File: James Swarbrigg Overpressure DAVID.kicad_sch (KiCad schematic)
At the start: 20 parts, among them J1 Screw_Terminal_01x02, J2 Screw_Terminal_01x02, J3 Fuse Holder 200mA, J4 Screw_Terminal_01x02, K1 G5V-2, Q1 BC184L, U2 TSR_1-2450, U3 LM358N

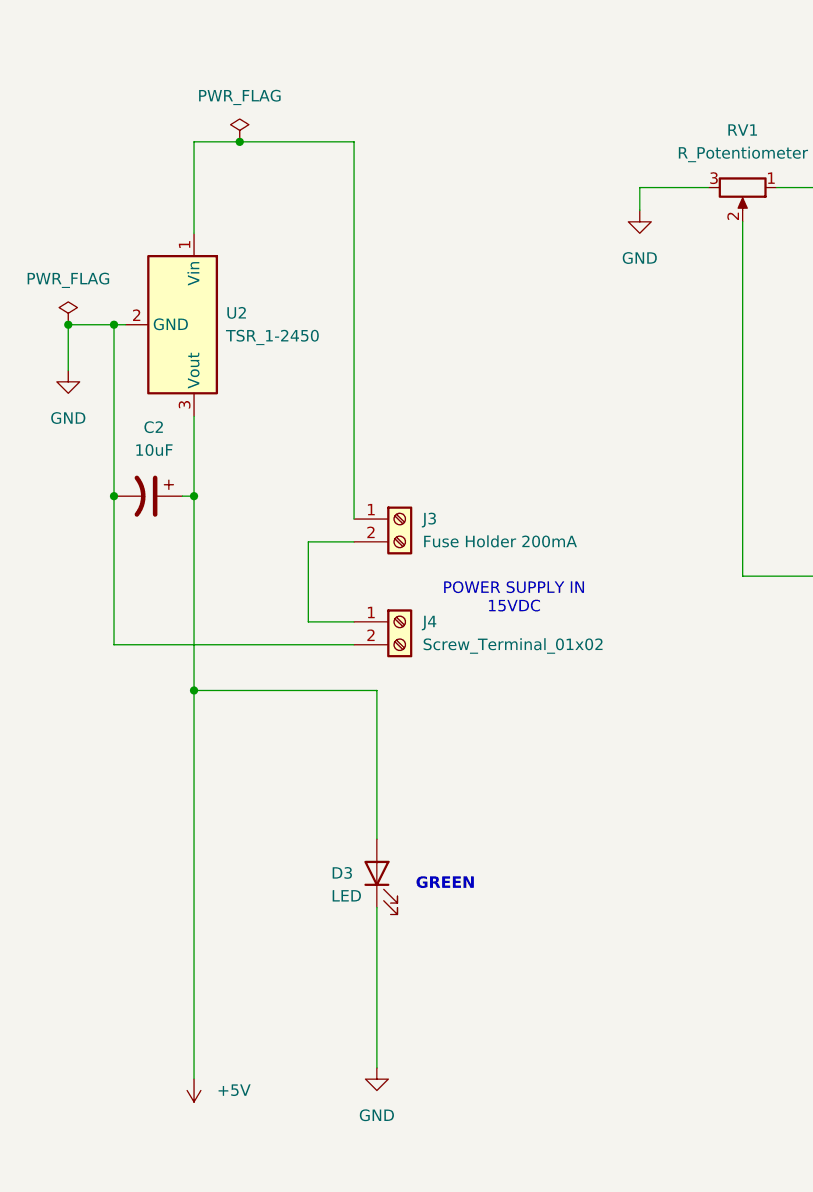
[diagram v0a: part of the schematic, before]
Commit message: Update overpressure cutout PCB and add Gerbers V1
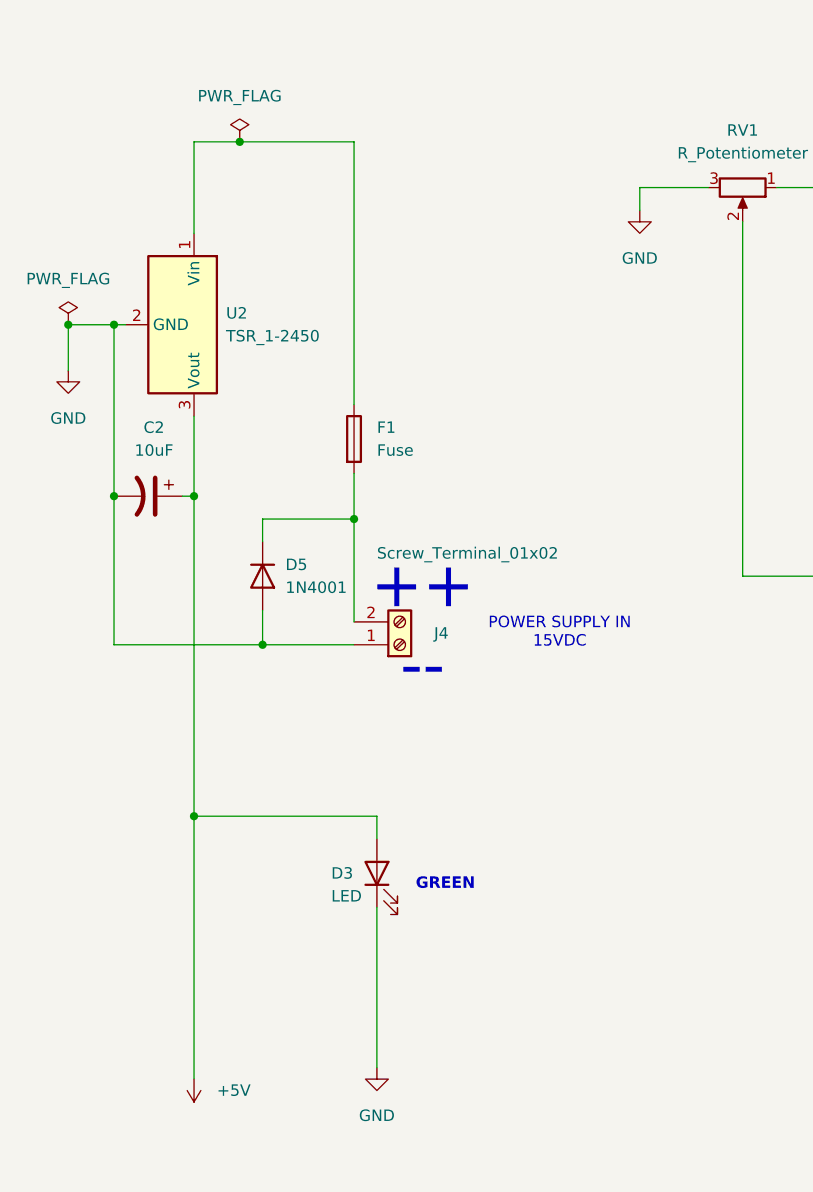
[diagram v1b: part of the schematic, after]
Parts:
- removed J3: Fuse Holder 200mA, Fuse:Fuseholder_Cylinder-5x20mm_Bulgin_FX0457_Horizontal_Closed, symbol Connector:Screw_Terminal_01x02
- added D5: 1N4001, Diode_THT:D_DO-41_SOD81_P10.16mm_Horizontal, symbol Diode:1N4001
- added F1: Fuse, Fuse:Fuseholder_Clip-5x20mm_Eaton_1A5601-01_Inline_P20.80x6.76mm_D1.70mm_Horizontal, symbol Device:Fuse
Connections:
- net GND: now also J4.1 (Pin_1), D5.2 (A); no longer J4.2 (Pin_2)
- net at U2.1 (Vin): now also F1.1
- new net: D5.1 (K), F1.2, J4.2 (Pin_2)
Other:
- note added: "++"
- note added: "--"
